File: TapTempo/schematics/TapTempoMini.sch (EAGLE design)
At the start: 58 parts, among them IC3 TL072D, Q2 8MHz, Q301 BC846, Q701 BC846, U1 STM32F100CBT6B, U2 NCP702

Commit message: fixed labels
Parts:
- added R502: 2k, resistor:R-EU_R0603
- added R503: 1k, resistor:R-EU_R0603
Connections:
- new net N$4: IC3B.-IN, R502.1, R503.1
- net DAC2: now also R503.2; no longer IC3B.+IN
- net GND: now also IC3B.+IN
- net N$3: now also R502.2; no longer IC3B.-IN
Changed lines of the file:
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@@
 <part name="JP5" library="SparkFun" deviceset="M02" device="PTH"/>
 <part name="GND18" library="supply1" deviceset="GND" device=""/>
+<part name="R502" library="resistor" deviceset="R-EU_" device="R0603" value="2k"/>
+<part name="R503" library="resistor" deviceset="R-EU_" device="R0603" value="1k"/>
+<part name="GND23" library="supply1" deviceset="GND" device=""/>
 </parts>
 <sheets>
@@
 <instance part="JP5" gate="G$1" x="210.82" y="78.74"/>
 <instance part="GND18" gate="1" x="220.98" y="73.66"/>
+<instance part="R502" gate="G$1" x="157.48" y="17.78"/>
+<instance part="R503" gate="G$1" x="139.7" y="7.62" rot="R180"/>
+<instance part="GND23" gate="1" x="147.32" y="-5.08"/>
 </instances>
 <busses>
@@
 <junction x="220.98" y="78.74"/>
 </segment>
+<segment>
+<pinref part="IC3" gate="B" pin="+IN"/>
+<pinref part="GND23" gate="1" pin="GND"/>
+<wire x1="149.86" y1="2.54" x2="147.32" y2="2.54" width="0.1524" layer="91"/>
+<wire x1="147.32" y1="2.54" x2="147.32" y2="-2.54" width="0.1524" layer="91"/>
+</segment>
 </net>
 <net name="-12V" class="0">
@@
 <pinref part="R403" gate="G$1" pin="2"/>
 <wire x1="124.46" y1="43.18" x2="134.62" y2="43.18" width="0.1524" layer="91"/>
-<label x="127" y="43.18" size="1.778" layer="95"/>
+<label x="124.46" y="43.18" size="1.778" layer="95"/>
 </segment>
 </net>
@@
 </segment>
 <segment>
-<label x="127" y="2.54" size="1.778" layer="95"/>
-<wire x1="124.46" y1="2.54" x2="149.86" y2="2.54" width="0.1524" layer="91"/>
-<pinref part="IC3" gate="B" pin="+IN"/>
+<wire x1="124.46" y1="7.62" x2="134.62" y2="7.62" width="0.1524" layer="91"/>
+<label x="124.46" y="7.62" size="1.778" layer="95"/>
+<pinref part="R503" gate="G$1" pin="2"/>
 </segment>
 </net>
@@
 <wire x1="170.18" y1="5.08" x2="167.64" y2="5.08" width="0.1524" layer="91"/>
 <wire x1="167.64" y1="5.08" x2="165.1" y2="5.08" width="0.1524" layer="91"/>
-<wire x1="167.64" y1="5.08" x2="167.64" y2="15.24" width="0.1524" layer="91"/>
+<wire x1="167.64" y1="5.08" x2="167.64" y2="17.78" width="0.1524" layer="91"/>
 <junction x="167.64" y="5.08"/>
-<wire x1="167.64" y1="15.24" x2="147.32" y2="15.24" width="0.1524" layer="91"/>
-<wire x1="147.32" y1="15.24" x2="147.32" y2="7.62" width="0.1524" layer="91"/>
-<pinref part="IC3" gate="B" pin="-IN"/>
-<wire x1="147.32" y1="7.62" x2="149.86" y2="7.62" width="0.1524" layer="91"/>
+<wire x1="167.64" y1="17.78" x2="162.56" y2="17.78" width="0.1524" layer="91"/>
+<pinref part="R502" gate="G$1" pin="2"/>
 </segment>
 </net>
@@
 </segment>
 </net>
+<net name="N$4" class="0">
+<segment>
+<pinref part="IC3" gate="B" pin="-IN"/>
+<pinref part="R502" gate="G$1" pin="1"/>
+<wire x1="152.4" y1="17.78" x2="147.32" y2="17.78" width="0.1524" layer="91"/>
+<wire x1="147.32" y1="17.78" x2="147.32" y2="7.62" width="0.1524" layer="91"/>
+<wire x1="147.32" y1="7.62" x2="149.86" y2="7.62" width="0.1524" layer="91"/>
+<pinref part="R503" gate="G$1" pin="1"/>
+<wire x1="147.32" y1="7.62" x2="144.78" y2="7.62" width="0.1524" layer="91"/>
+<junction x="147.32" y="7.62"/>
+</segment>
+</net>

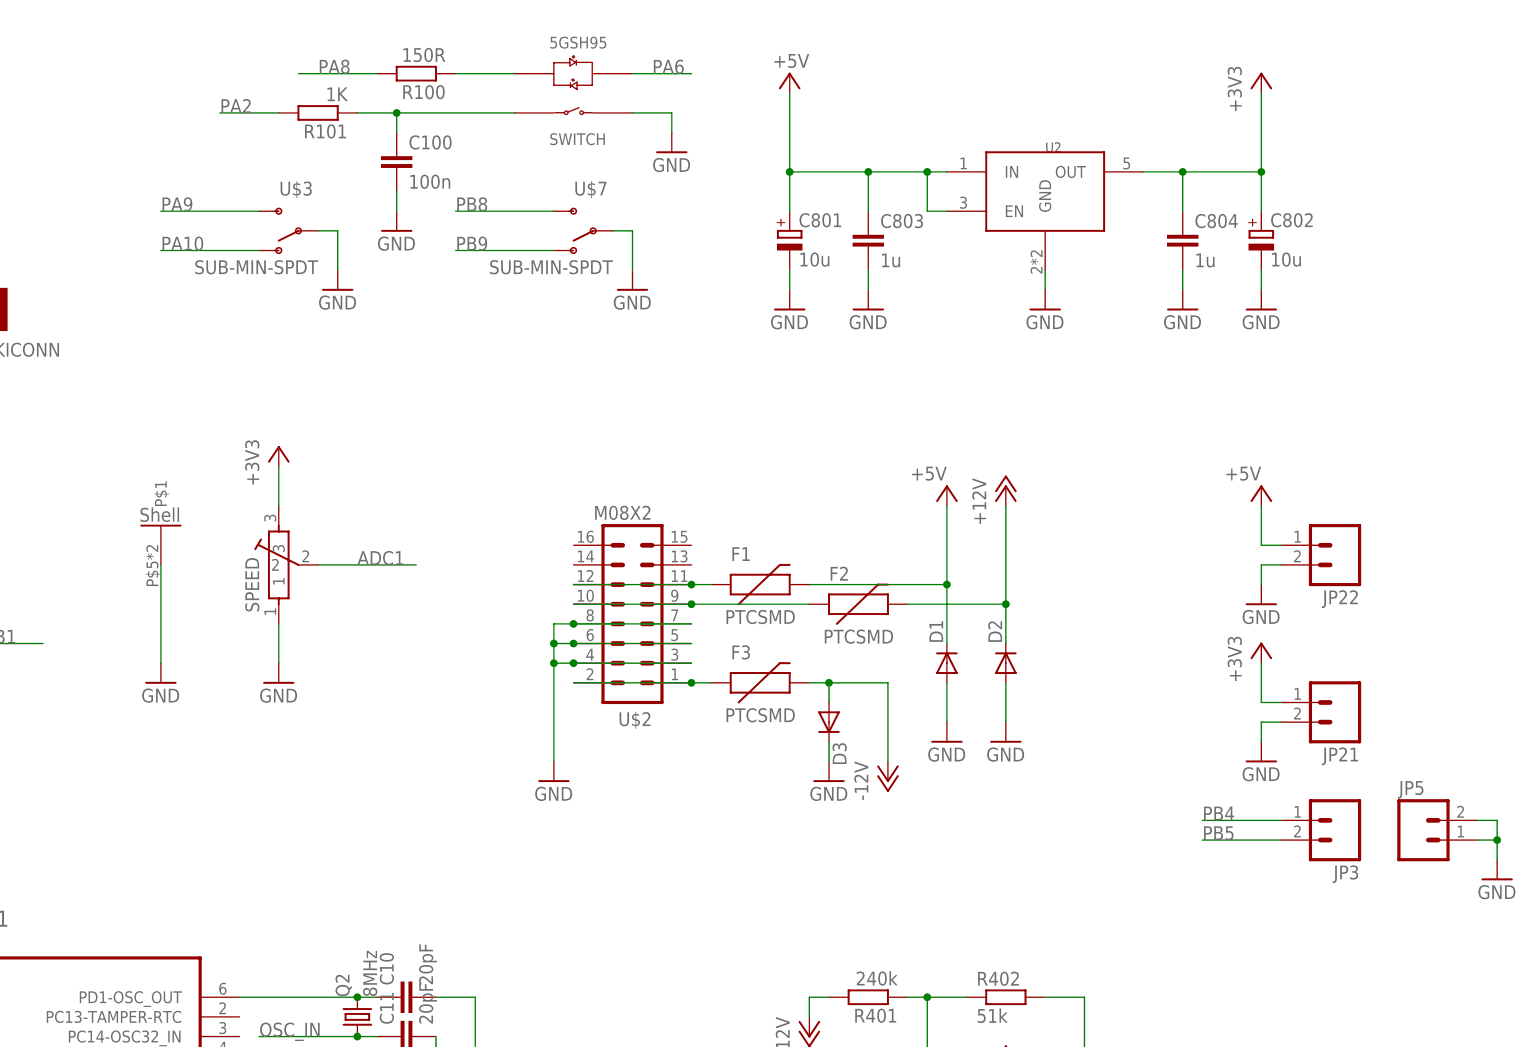
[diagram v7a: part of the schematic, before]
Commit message: added pull-up resistor on PB8
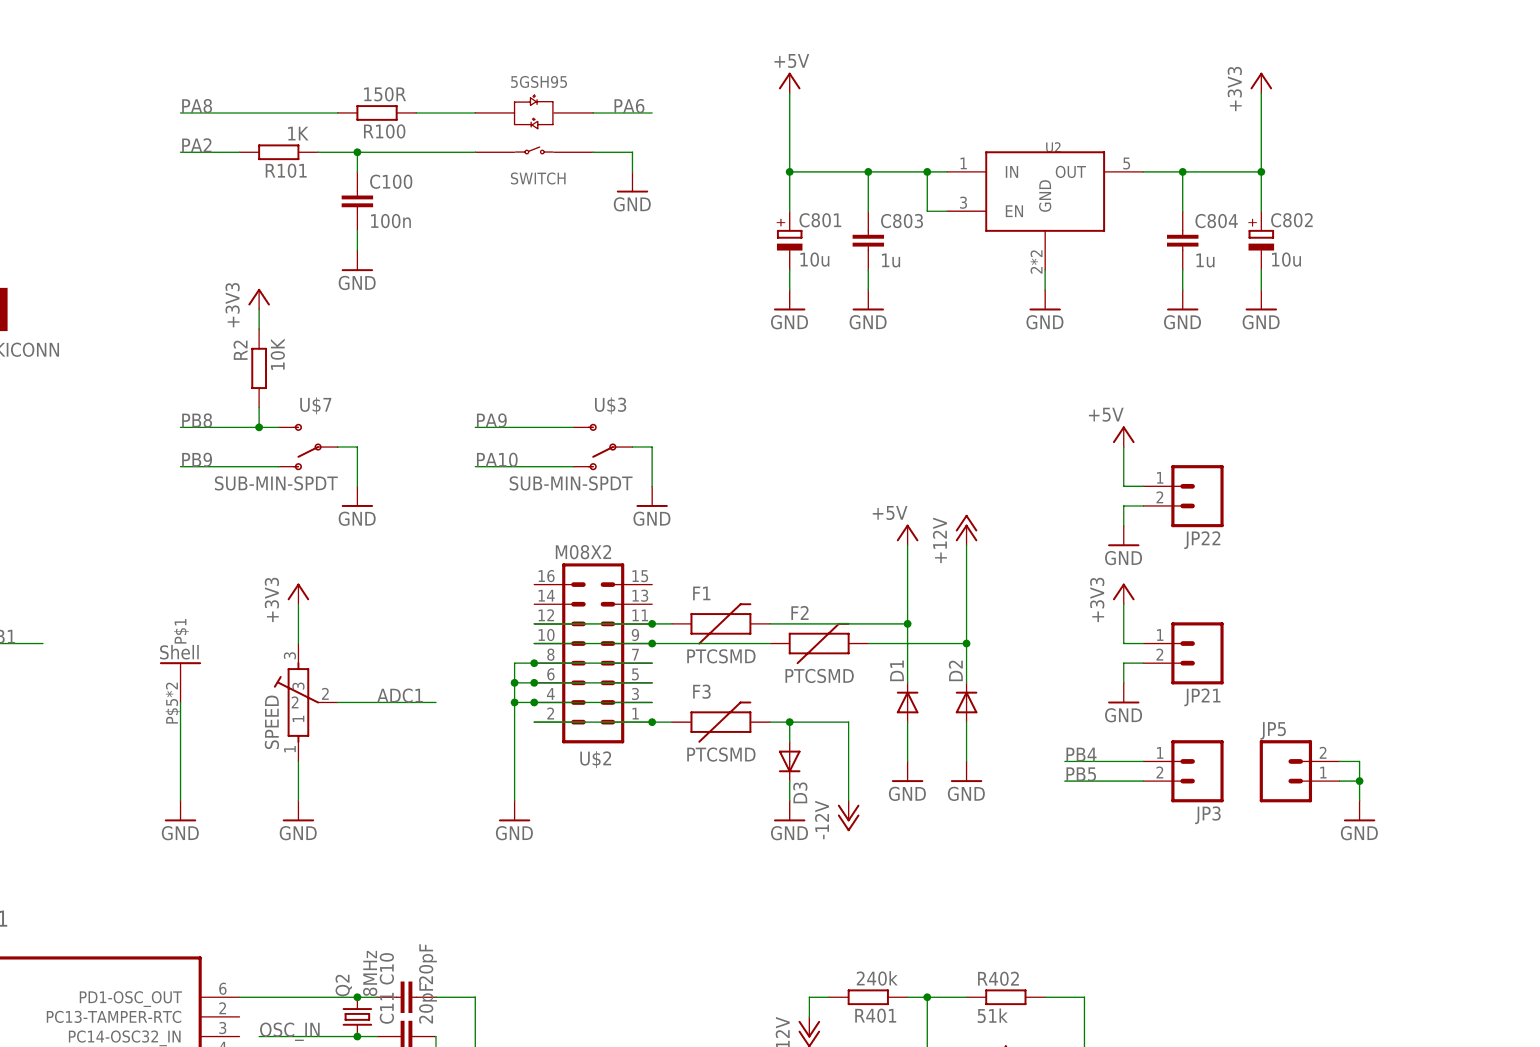
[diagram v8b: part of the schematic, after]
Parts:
- added R2: 10K, resistor:R-EU_R0603
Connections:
- net +3V3: now also R2.1
- net PB8: now also R2.2
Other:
- moved on the sheet: C100, D1, D2, D3, F1, F2, F3, JP21, JP22, JP3, JP5, R100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
